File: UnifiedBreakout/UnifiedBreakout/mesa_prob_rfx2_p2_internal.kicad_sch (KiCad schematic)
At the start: 1 part, among them J10 MESA P2 INTERNAL IO

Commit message: WIP updating breakout for electrical enclosure
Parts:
- J10: symbol UnifiedBreakout-rescue:DB25_Female_MountingHoles-Connector -> Connector:DB25_Receptacle_MountingHoles; Alternative MPN L77SDB25SA4CH4F -> (none); Farnell PN (none) -> 2059751; MPN ID25S33E4GX00LF -> 5747846-4; Manufacturer Amphenol -> AMP - TE Connectivity
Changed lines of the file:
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@@
-(kicad_sch (version 20211123) (generator eeschema)
+(kicad_sch (version 20230121) (generator eeschema)
   (paper "A4")
   (junction (at 130.81 135.89) (diameter 0.9144) (color 0 0 0 0)
@@
   )
   (wire (pts (xy 127 88.9) (xy 127 113.03))
-    (stroke (width 0) (type solid) (color 0 0 0 0))
+    (stroke (width 0) (type solid))
   )
   (wire (pts (xy 130.81 135.89) (xy 130.81 107.95))
-    (stroke (width 0) (type solid) (color 0 0 0 0))
+    (stroke (width 0) (type solid))
   )
   (wire (pts (xy 130.81 97.79) (xy 130.81 102.87))
-    (stroke (width 0) (type solid) (color 0 0 0 0))
+    (stroke (width 0) (type solid))
   )
   (wire (pts (xy 127 113.03) (xy 127 118.11))
-    (stroke (width 0) (type solid) (color 0 0 0 0))
+    (stroke (width 0) (type solid))
   )
   (wire (pts (xy 130.81 92.71) (xy 130.81 97.79))
-    (stroke (width 0) (type solid) (color 0 0 0 0))
+    (stroke (width 0) (type solid))
   )
   (wire (pts (xy 161.29 123.19) (xy 127 123.19))
-    (stroke (width 0) (type solid) (color 0 0 0 0))
+    (stroke (width 0) (type solid))
   )
   (wire (pts (xy 130.81 97.79) (xy 161.29 97.79))
-    (stroke (width 0) (type solid) (color 0 0 0 0))
+    (stroke (width 0) (type solid))
   )
   (wire (pts (xy 127 123.19) (xy 127 128.27))
-    (stroke (width 0) (type solid) (color 0 0 0 0))
+    (stroke (width 0) (type solid))
   )
   (wire (pts (xy 130.81 102.87) (xy 130.81 107.95))
-    (stroke (width 0) (type solid) (color 0 0 0 0))
+    (stroke (width 0) (type solid))
   )
   (wire (pts (xy 161.29 102.87) (xy 130.81 102.87))
-    (stroke (width 0) (type solid) (color 0 0 0 0))
+    (stroke (width 0) (type solid))
   )
   (wire (pts (xy 161.29 113.03) (xy 127 113.03))
-    (stroke (width 0) (type solid) (color 0 0 0 0))
+    (stroke (width 0) (type solid))
   )
   (wire (pts (xy 127 118.11) (xy 161.29 118.11))
-    (stroke (width 0) (type solid) (color 0 0 0 0))
+    (stroke (width 0) (type solid))
   )
   (wire (pts (xy 161.29 92.71) (xy 130.81 92.71))
-    (stroke (width 0) (type solid) (color 0 0 0 0))
+    (stroke (width 0) (type solid))
   )
   (wire (pts (xy 130.81 135.89) (xy 168.91 135.89))
-    (stroke (width 0) (type solid) (color 0 0 0 0))
+    (stroke (width 0) (type solid))
   )
   (wire (pts (xy 127 128.27) (xy 161.29 128.27))
-    (stroke (width 0) (type solid) (color 0 0 0 0))
+    (stroke (width 0) (type solid))
   )
   (wire (pts (xy 130.81 107.95) (xy 161.29 107.95))
-    (stroke (width 0) (type solid) (color 0 0 0 0))
+    (stroke (width 0) (type solid))
   )
   (wire (pts (xy 127 118.11) (xy 127 123.19))
-    (stroke (width 0) (type solid) (color 0 0 0 0))
+    (stroke (width 0) (type solid))
   )
   (wire (pts (xy 130.81 139.7) (xy 130.81 135.89))
-    (stroke (width 0) (type solid) (color 0 0 0 0))
+    (stroke (width 0) (type solid))
   )
-  (hierarchical_label "IO_31_QUAD_01_A" (shape input) (at 161.29 120.65 180)
+  (hierarchical_label "IO_31_QUAD_01_A" (shape input) (at 161.29 120.65 180) (fields_autoplaced)
     (effects (font (size 1.27 1.27)) (justify right))
   )
-  (hierarchical_label "IO_24" (shape bidirectional) (at 161.29 87.63 180)
+  (hierarchical_label "IO_24" (shape bidirectional) (at 161.29 87.63 180) (fields_autoplaced)
     (effects (font (size 1.27 1.27)) (justify right))
   )
-  (hierarchical_label "IO_27_STEPGEN_06_DIR" (shape output) (at 161.29 100.33 180)
+  (hierarchical_label "IO_27_STEPGEN_06_DIR" (shape output) (at 161.29 100.33 180) (fields_autoplaced)
     (effects (font (size 1.27 1.27)) (justify right))
   )
-  (hierarchical_label "IO_33_QUAD_01_IDX" (shape input) (at 161.29 130.81 180)
+  (hierarchical_label "IO_33_QUAD_01_IDX" (shape input) (at 161.29 130.81 180) (fields_autoplaced)
     (effects (font (size 1.27 1.27)) (justify right))
   )
-  (hierarchical_label "IO_29_STEPGEN_07_DIR" (shape output) (at 161.29 110.49 180)
+  (hierarchical_label "IO_29_STEPGEN_07_DIR" (shape output) (at 161.29 110.49 180) (fields_autoplaced)
     (effects (font (size 1.27 1.27)) (justify right))
   )
-  (hierarchical_label "IO_19_STEPGEN_04_STEP" (shape output) (at 161.29 74.93 180)
+  (hierarchical_label "IO_19_STEPGEN_04_STEP" (shape output) (at 161.29 74.93 180) (fields_autoplaced)
     (effects (font (size 1.27 1.27)) (justify right))
   )
-  (hierarchical_label "IO_26_STEPGEN_06_STEP" (shape output) (at 161.29 95.25 180)
+  (hierarchical_label "IO_26_STEPGEN_06_STEP" (shape output) (at 161.29 95.25 180) (fields_autoplaced)
     (effects (font (size 1.27 1.27)) (justify right))
   )
-  (hierarchical_label "IO_20" (shape bidirectional) (at 161.29 77.47 180)
+  (hierarchical_label "IO_20" (shape bidirectional) (at 161.29 77.47 180) (fields_autoplaced)
     (effects (font (size 1.27 1.27)) (justify right))
   )
-  (hierarchical_label "IO_32_QUAD_01_B" (shape input) (at 161.29 125.73 180)
+  (hierarchical_label "IO_32_QUAD_01_B" (shape input) (at 161.29 125.73 180) (fields_autoplaced)
     (effects (font (size 1.27 1.27)) (justify right))
   )
-  (hierarchical_label "IO_21_STEPGEN_04_DIR" (shape output) (at 161.29 80.01 180)
+  (hierarchical_label "IO_21_STEPGEN_04_DIR" (shape output) (at 161.29 80.01 180) (fields_autoplaced)
     (effects (font (size 1.27 1.27)) (justify right))
   )
-  (hierarchical_label "MESA_5V" (shape passive) (at 127 88.9 90)
+  (hierarchical_label "MESA_5V" (shape passive) (at 127 88.9 90) (fields_autoplaced)
     (effects (font (size 1.27 1.27)) (justify left))
   )
-  (hierarchical_label "GND" (shape passive) (at 130.81 139.7 270)
+  (hierarchical_label "GND" (shape passive) (at 130.81 139.7 270) (fields_autoplaced)
     (effects (font (size 1.27 1.27)) (justify right))
   )
-  (hierarchical_label "IO_18_PWMGEN_01_PWM" (shape output) (at 161.29 72.39 180)
+  (hierarchical_label "IO_18_PWMGEN_01_PWM" (shape output) (at 161.29 72.39 180) (fields_autoplaced)
     (effects (font (size 1.27 1.27)) (justify right))
   )
-  (hierarchical_label "IO_22_PWMGEN_01_DIR" (shape output) (at 161.29 82.55 180)
+  (hierarchical_label "IO_22_PWMGEN_01_DIR" (shape output) (at 161.29 82.55 180) (fields_autoplaced)
     (effects (font (size 1.27 1.27)) (justify right))
   )
-  (hierarchical_label "IO_30" (shape bidirectional) (at 161.29 115.57 180)
+  (hierarchical_label "IO_30" (shape bidirectional) (at 161.29 115.57 180) (fields_autoplaced)
     (effects (font (size 1.27 1.27)) (justify right))
   )
-  (hierarchical_label "IO_23_STEPGEN_05_STEP" (shape output) (at 161.29 85.09 180)
+  (hierarchical_label "IO_23_STEPGEN_05_STEP" (shape output) (at 161.29 85.09 180) (fields_autoplaced)
     (effects (font (size 1.27 1.27)) (justify right))
   )
-  (hierarchical_label "IO_17" (shape bidirectional) (at 161.29 69.85 180)
+  (hierarchical_label "IO_17" (shape bidirectional) (at 161.29 69.85 180) (fields_autoplaced)
     (effects (font (size 1.27 1.27)) (justify right))
   )
-  (hierarchical_label "IO_28_STEPGEN_07_STEP" (shape output) (at 161.29 105.41 180)
+  (hierarchical_label "IO_28_STEPGEN_07_STEP" (shape output) (at 161.29 105.41 180) (fields_autoplaced)
     (effects (font (size 1.27 1.27)) (justify right))
   )
-  (hierarchical_label "IO_25_STEPGEN_05_DIR" (shape output) (at 161.29 90.17 180)
+  (hierarchical_label "IO_25_STEPGEN_05_DIR" (shape output) (at 161.29 90.17 180) (fields_autoplaced)
     (effects (font (size 1.27 1.27)) (justify right))
   )
-  (symbol (lib_id "UnifiedBreakout-rescue:DB25_Female_MountingHoles-Connector") (at 168.91 100.33 0) (unit 1)
-    (in_bom yes) (on_board yes)
-    (property "Reference" "J10" (id 0) (at 173.482 100.2792 0)
+  (symbol (lib_id "Connector:DB25_Receptacle_MountingHoles") (at 168.91 100.33 0) (unit 1)
+    (in_bom yes) (on_board yes) (dnp no)
+    (property "Reference" "J10" (at 173.482 100.2792 0)
       (effects (font (size 1.27 1.27)) (justify left))
     )
-    (property "Value" "MESA P2 INTERNAL IO" (id 1) (at 173.482 102.5906 0)
+    (property "Value" "MESA P2 INTERNAL IO" (at 173.482 102.5906 0)
       (effects (font (size 1.27 1.27)) (justify left))
     )
-    (property "Footprint" "Connector_Dsub:DSUB-25_Female_Horizontal_P2.77x2.84mm_EdgePinOffset7.70mm_Housed_MountingHolesOffset9.12mm" (id 2) (at 168.91 100.33 0)
+    (property "Footprint" "Connector_Dsub:DSUB-25_Female_Horizontal_P2.77x2.84mm_EdgePinOffset7.70mm_Housed_MountingHolesOffset9.12mm" (at 168.91 100.33 0)
       (effects (font (size 1.27 1.27)) hide)
     )
-    (property "Datasheet" " ~" (id 3) (at 168.91 100.33 0)
+    (property "Datasheet" " ~" (at 168.91 100.33 0)
       (effects (font (size 1.27 1.27)) hide)
     )
-    (property "Alternative MPN" "L77SDB25SA4CH4F " (id 4) (at 168.91 100.33 0)
+    (property "Alternative MPN" "" (at 168.91 100.33 0)
       (effects (font (size 1.27 1.27)) hide)
     )
-    (property "MPN" "ID25S33E4GX00LF" (id 5) (at 168.91 100.33 0)
+    (property "MPN" "5747846-4 " (at 168.91 100.33 0)
       (effects (font (size 1.27 1.27)) hide)
     )
-    (property "Manufacturer" "Amphenol" (id 6) (at 168.91 100.33 0)
+    (property "Manufacturer" "AMP - TE Connectivity" (at 168.91 100.33 0)
+      (effects (font (size 1.27 1.27)) hide)
+    )
+    (property "Farnell PN" "2059751" (at 168.91 100.33 0)
       (effects (font (size 1.27 1.27)) hide)
     )
@@
     (pin "8")
     (pin "9")
+    (instances
+      (project "UnifiedBreakout"
+        (path "/e63e39d7-6ac0-4ffd-8aa3-1841a4541b55/00000000-0000-0000-0000-00005e96eb73"
+          (reference "J10") (unit 1)
+        )
+      )
+    )
   )
 )

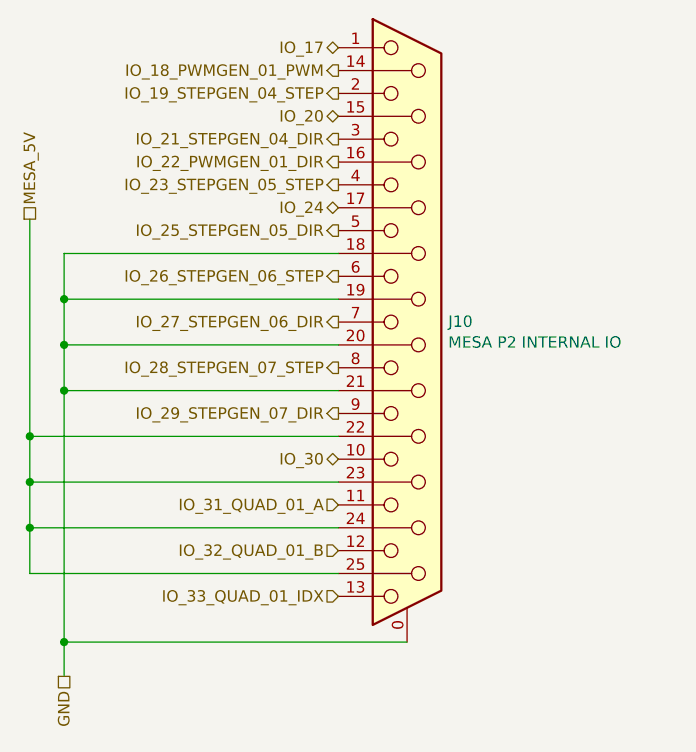
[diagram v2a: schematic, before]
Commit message: Add dual level DB25
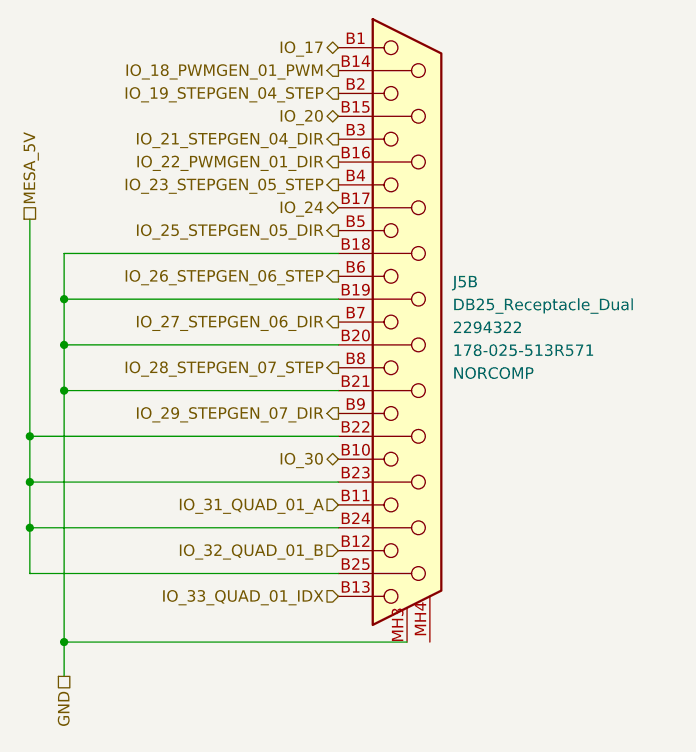
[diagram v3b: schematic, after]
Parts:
- removed J10: MESA P2 INTERNAL IO, Connector_Dsub:DSUB-25_Female_Horizontal_P2.77x2.84mm_EdgePinOffset7.70mm_Housed_MountingHolesOffset9.12mm, symbol Connector:DB25_Receptacle_MountingHoles
- added J5: DB25_Receptacle_Dual, UnifiedBreakout:NorComp-Dual-DB25, symbol UnifiedBreakout:DB25_Receptacle_Dual
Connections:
- net GND: now also J5.B18, J5.B19, J5.B20, J5.B21, J5.MH3
- net IO_17: now also J5.B1
- net IO_18_PWMGEN_01_PWM: now also J5.B14
- net IO_19_STEPGEN_04_STEP: now also J5.B2
- net IO_20: now also J5.B15
- net IO_21_STEPGEN_04_DIR: now also J5.B3
- net IO_22_PWMGEN_01_DIR: now also J5.B16
- net IO_23_STEPGEN_05_STEP: now also J5.B4
- net IO_24: now also J5.B17
- net IO_25_STEPGEN_05_DIR: now also J5.B5
- net IO_26_STEPGEN_06_STEP: now also J5.B6
- net IO_27_STEPGEN_06_DIR: now also J5.B7
- net IO_28_STEPGEN_07_STEP: now also J5.B8
- net IO_29_STEPGEN_07_DIR: now also J5.B9
- net IO_30: now also J5.B10
- net IO_31_QUAD_01_A: now also J5.B11
- net IO_32_QUAD_01_B: now also J5.B12
- net IO_33_QUAD_01_IDX: now also J5.B13
- net MESA_5V: now also J5.B22, J5.B23, J5.B24, J5.B25
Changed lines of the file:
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@@
     (effects (font (size 1.27 1.27)) (justify right))
   )
-  (symbol (lib_id "Connector:DB25_Receptacle_MountingHoles") (at 168.91 100.33 0) (unit 1)
-    (in_bom yes) (on_board yes) (dnp no)
-    (property "Reference" "J10" (at 173.482 100.2792 0)
+  (symbol (lib_id "UnifiedBreakout:DB25_Receptacle_Dual") (at 168.91 100.33 0) (unit 2)
+    (in_bom yes) (on_board yes) (dnp no) (fields_autoplaced)
+    (property "Reference" "J5" (at 173.99 95.885 0)
       (effects (font (size 1.27 1.27)) (justify left))
     )
-    (property "Value" "MESA P2 INTERNAL IO" (at 173.482 102.5906 0)
+    (property "Value" "DB25_Receptacle_Dual" (at 173.99 98.425 0)
       (effects (font (size 1.27 1.27)) (justify left))
     )
-    (property "Footprint" "Connector_Dsub:DSUB-25_Female_Horizontal_P2.77x2.84mm_EdgePinOffset7.70mm_Housed_MountingHolesOffset9.12mm" (at 168.91 100.33 0)
+    (property "Footprint" "UnifiedBreakout:NorComp-Dual-DB25" (at 168.91 100.33 0)
       (effects (font (size 1.27 1.27)) hide)
     )
@@
       (effects (font (size 1.27 1.27)) hide)
     )
-    (property "Alternative MPN" "" (at 168.91 100.33 0)
-      (effects (font (size 1.27 1.27)) hide)
+    (property "Farnell PN" "2294322" (at 173.99 100.965 0)
+      (effects (font (size 1.27 1.27)) (justify left))
     )
-    (property "MPN" "5747846-4 " (at 168.91 100.33 0)
-      (effects (font (size 1.27 1.27)) hide)
+    (property "MPN" "178-025-513R571" (at 173.99 103.505 0)
+      (effects (font (size 1.27 1.27)) (justify left))
     )
-    (property "Manufacturer" "AMP - TE Connectivity" (at 168.91 100.33 0)
-      (effects (font (size 1.27 1.27)) hide)
+    (property "Manufacturer" "NORCOMP" (at 173.99 106.045 0)
+      (effects (font (size 1.27 1.27)) (justify left))
     )
-    (property "Farnell PN" "2059751" (at 168.91 100.33 0)
-      (effects (font (size 1.27 1.27)) hide)
-    )
-    (pin "0")
-    (pin "1")
-    (pin "10")
-    (pin "11")
-    (pin "12")
-    (pin "13")
-    (pin "14")
-    (pin "15")
-    (pin "16")
-    (pin "17")
-    (pin "18")
-    (pin "19")
-    (pin "2")
-    (pin "20")
-    (pin "21")
-    (pin "22")
-    (pin "23")
-    (pin "24")
-    (pin "25")
-    (pin "3")
-    (pin "4")
-    (pin "5")
-    (pin "6")
-    (pin "7")
-    (pin "8")
-    (pin "9")
+    (pin "A1")
+    (pin "A10")
+    (pin "A11")
+    (pin "A12")
+    (pin "A13")
+    (pin "A14")
+    (pin "A15")
+    (pin "A16")
+    (pin "A17")
+    (pin "A18")
+    (pin "A19")
+    (pin "A2")
+    (pin "A20")
+    (pin "A21")
+    (pin "A22")
+    (pin "A23")
+    (pin "A24")
+    (pin "A25")
+    (pin "A3")
+    (pin "A4")
+    (pin "A5")
+    (pin "A6")
+    (pin "A7")
+    (pin "A8")
+    (pin "A9")
+    (pin "MH1")
+    (pin "MH2")
+    (pin "B1")
+    (pin "B10")
+    (pin "B11")
+    (pin "B12")
+    (pin "B13")
+    (pin "B14")
+    (pin "B15")
+    (pin "B16")
+    (pin "B17")
+    (pin "B18")
+    (pin "B19")
+    (pin "B2")
+    (pin "B20")
+    (pin "B21")
+    (pin "B22")
+    (pin "B23")
+    (pin "B24")
+    (pin "B25")
+    (pin "B3")
+    (pin "B4")
+    (pin "B5")
+    (pin "B6")
+    (pin "B7")
+    (pin "B8")
+    (pin "B9")
+    (pin "MH3")
+    (pin "MH4")
     (instances
       (project "UnifiedBreakout"
         (path "/e63e39d7-6ac0-4ffd-8aa3-1841a4541b55/00000000-0000-0000-0000-00005e96eb73"
-          (reference "J10") (unit 1)
+          (reference "J5") (unit 2)
         )
       )

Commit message: Update IO and opto
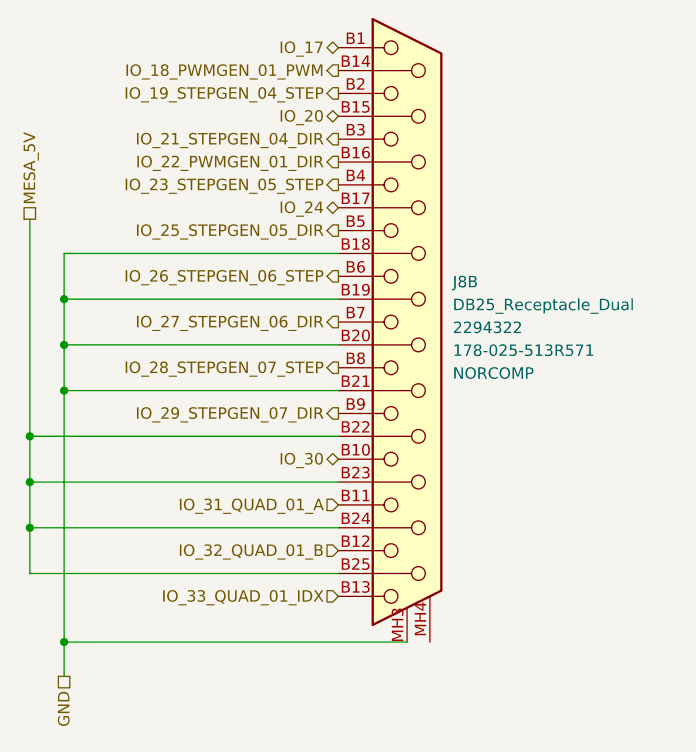
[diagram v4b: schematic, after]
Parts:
- renumbered J5 to J8
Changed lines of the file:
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@@
   (symbol (lib_id "UnifiedBreakout:DB25_Receptacle_Dual") (at 168.91 100.33 0) (unit 2)
     (in_bom yes) (on_board yes) (dnp no) (fields_autoplaced)
-    (property "Reference" "J5" (at 173.99 95.885 0)
+    (property "Reference" "J8" (at 173.99 95.885 0)
       (effects (font (size 1.27 1.27)) (justify left))
     )
@@
       (project "UnifiedBreakout"
         (path "/e63e39d7-6ac0-4ffd-8aa3-1841a4541b55/00000000-0000-0000-0000-00005e96eb73"
-          (reference "J5") (unit 2)
+          (reference "J8") (unit 2)
         )
       )

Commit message: Started some layout
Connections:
- net GND: now also J8.MH4
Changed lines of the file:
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@@
   (junction (at 127 118.11) (diameter 0.9144) (color 0 0 0 0)
+  )
+  (junction (at 168.91 135.89) (diameter 0) (color 0 0 0 0)
   )
   (junction (at 130.81 107.95) (diameter 0.9144) (color 0 0 0 0)
@@
     (stroke (width 0) (type solid))
   )
+  (wire (pts (xy 168.91 135.89) (xy 171.45 135.89))
+    (stroke (width 0) (type default))
+  )
   (wire (pts (xy 130.81 102.87) (xy 130.81 107.95))

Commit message: Some layout
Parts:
- renumbered J8 to J10
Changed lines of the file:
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@@
   (symbol (lib_id "UnifiedBreakout:DB25_Receptacle_Dual") (at 168.91 100.33 0) (unit 2)
     (in_bom yes) (on_board yes) (dnp no) (fields_autoplaced)
-    (property "Reference" "J8" (at 173.99 95.885 0)
+    (property "Reference" "J10" (at 173.99 95.885 0)
       (effects (font (size 1.27 1.27)) (justify left))
     )
@@
       (project "UnifiedBreakout"
         (path "/e63e39d7-6ac0-4ffd-8aa3-1841a4541b55/00000000-0000-0000-0000-00005e96eb73"
-          (reference "J8") (unit 2)
+          (reference "J10") (unit 2)
         )
       )
